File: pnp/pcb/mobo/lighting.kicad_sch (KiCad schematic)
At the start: 2 parts, among them J13 DOWNWARDS_LIGHT, J14 UPWARDS_LIGHT

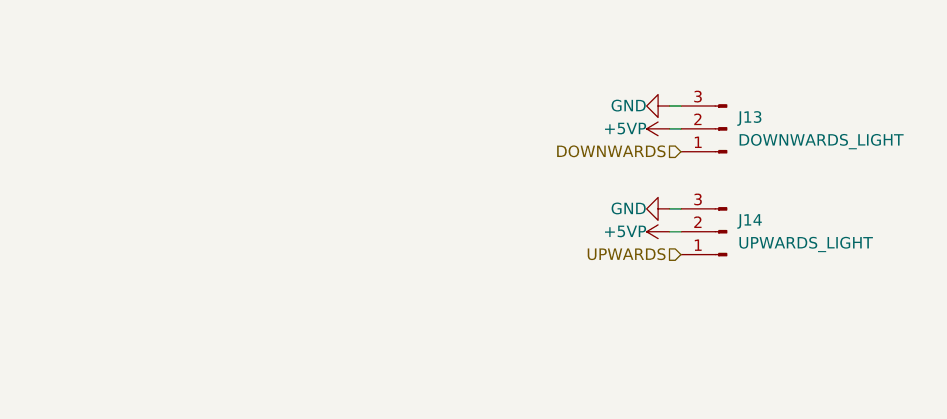
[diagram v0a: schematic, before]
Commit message: Mobo V4A Redesign
Some EMC improvements to schematics.
Reassigned MCU Pins for HW-PWM support.
Changes are still marked with text in the schematics.
Complete PCB Layout reworked
Status: Needs to be verified, and cleaned up a little, but DRC is running green.
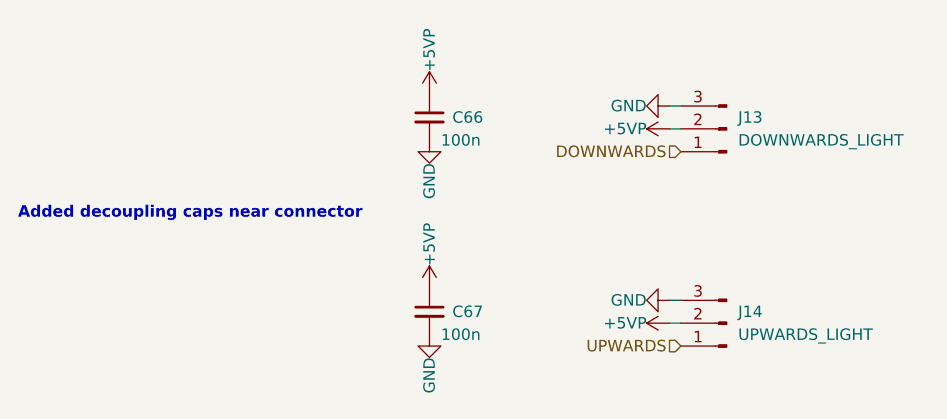
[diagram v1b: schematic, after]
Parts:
- added C66, C67: 100n, Capacitor_SMD:C_0805_2012Metric, symbol Device:C_Small
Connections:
- net +5VP: now also C66.1, C67.1
- net GND: now also C66.2, C67.2
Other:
- note added: "Added decoupling caps near connector"
- moved on the sheet: J14
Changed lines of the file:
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@@
   (title_block
     (title "LumenPnP Motherboard")
-    (date "2022-03-29")
+    (date "2022-09-09")
+    (rev "004A")
     (company "Opulo")
-  )
-  (wire (pts (xy 143.51 105.41) (xy 144.78 105.41))
+    (comment 1 "Reengineered by Magpie")
+  )
+  (wire (pts (xy 143.51 115.57) (xy 144.78 115.57))
     (stroke (width 0) (type default) (color 0 0 0 0))
   )
@@
     (stroke (width 0) (type default) (color 0 0 0 0))
   )
-  (wire (pts (xy 143.51 107.95) (xy 144.78 107.95))
+  (wire (pts (xy 143.51 118.11) (xy 144.78 118.11))
     (stroke (width 0) (type default) (color 0 0 0 0))
   )
@@
     (stroke (width 0) (type default) (color 0 0 0 0))
   )
-  (hierarchical_label "UPWARDS" (shape input) (at 144.78 110.49 180)
+  (text "Added decoupling caps near connector" (at 71.12 106.68 0)
+    (effects (font (size 1.27 1.27) (thickness 0.254) bold) (justify left bottom))
+  )
+  (hierarchical_label "UPWARDS" (shape input) (at 144.78 120.65 180)
     (effects (font (size 1.27 1.27)) (justify right))
   )
@@
     (pin "3")
   )
-  (symbol (lib_id "Connector:Conn_01x03_Male") (at 149.86 107.95 180) (unit 1)
-    (in_bom yes) (on_board yes)
-    (property "Reference" "J14" (id 0) (at 151.13 106.68 0)
-      (effects (font (size 1.27 1.27)) (justify right))
-    )
-    (property "Value" "UPWARDS_LIGHT" (id 1) (at 151.13 109.22 0)
-      (effects (font (size 1.27 1.27)) (justify right))
-    )
-    (property "Footprint" "Connector_JST:JST_XH_B3B-XH-A_1x03_P2.50mm_Vertical" (id 2) (at 149.86 107.95 0)
-      (effects (font (size 1.27 1.27)) hide)
-    )
-    (property "Datasheet" "" (id 3) (at 149.86 107.95 0)
-      (effects (font (size 1.27 1.27)) hide)
-    )
-    (property "LCSC" "C2316" (id 4) (at 149.86 107.95 0)
-      (effects (font (size 1.27 1.27)) hide)
-    )
-    (property "JLCPCB" "C2316" (id 5) (at 149.86 107.95 0)
-      (effects (font (size 1.27 1.27)) hide)
-    )
-    (property "Digikey" "455-2248-ND" (id 6) (at 149.86 107.95 0)
+  (symbol (lib_id "Connector:Conn_01x03_Male") (at 149.86 118.11 180) (unit 1)
+    (in_bom yes) (on_board yes)
+    (property "Reference" "J14" (id 0) (at 151.13 116.84 0)
+      (effects (font (size 1.27 1.27)) (justify right))
+    )
+    (property "Value" "UPWARDS_LIGHT" (id 1) (at 151.13 119.38 0)
+      (effects (font (size 1.27 1.27)) (justify right))
+    )
+    (property "Footprint" "Connector_JST:JST_XH_B3B-XH-A_1x03_P2.50mm_Vertical" (id 2) (at 149.86 118.11 0)
+      (effects (font (size 1.27 1.27)) hide)
+    )
+    (property "Datasheet" "" (id 3) (at 149.86 118.11 0)
+      (effects (font (size 1.27 1.27)) hide)
+    )
+    (property "LCSC" "C2316" (id 4) (at 149.86 118.11 0)
+      (effects (font (size 1.27 1.27)) hide)
+    )
+    (property "JLCPCB" "C2316" (id 5) (at 149.86 118.11 0)
+      (effects (font (size 1.27 1.27)) hide)
+    )
+    (property "Digikey" "455-2248-ND" (id 6) (at 149.86 118.11 0)
       (effects (font (size 1.27 1.27)) hide)
     )
@@
     (pin "3")
   )
+  (symbol (lib_id "power:GND") (at 116.84 97.79 0) (unit 1)
+    (in_bom yes) (on_board yes)
+    (property "Reference" "#PWR023" (id 0) (at 116.84 104.14 0)
+      (effects (font (size 1.27 1.27)) hide)
+    )
+    (property "Value" "GND" (id 1) (at 116.84 100.33 90)
+      (effects (font (size 1.27 1.27)) (justify right))
+    )
+    (property "Footprint" "" (id 2) (at 116.84 97.79 0)
+      (effects (font (size 1.27 1.27)) hide)
+    )
+    (property "Datasheet" "" (id 3) (at 116.84 97.79 0)
+      (effects (font (size 1.27 1.27)) hide)
+    )
+    (pin "1")
+  )
+  (symbol (lib_id "Device:C_Small") (at 116.84 116.84 0) (unit 1)
+    (in_bom yes) (on_board yes)
+    (property "Reference" "C67" (id 0) (at 119.38 116.84 0)
+      (effects (font (size 1.27 1.27)) (justify left))
+    )
+    (property "Value" "100n" (id 1) (at 118.11 119.38 0)
+      (effects (font (size 1.27 1.27)) (justify left))
+    )
+    (property "Footprint" "Capacitor_SMD:C_0805_2012Metric" (id 2) (at 116.84 116.84 0)
+      (effects (font (size 1.27 1.27)) hide)
+    )
+    (property "Datasheet" "" (id 3) (at 116.84 116.84 0)
+      (effects (font (size 1.27 1.27)) hide)
+    )
+    (property "Digikey" "1276-1180-1-ND" (id 4) (at 116.84 116.84 0)
+      (effects (font (size 1.27 1.27)) hide)
+    )
+    (property "JLCPCB" "C49678" (id 5) (at 116.84 116.84 0)
+      (effects (font (size 1.27 1.27)) hide)
+    )
+    (property "LCSC" "C360619" (id 6) (at 116.84 116.84 0)
+      (effects (font (size 1.27 1.27)) hide)
+    )
+    (property "Mouser" "581-08055C104K" (id 7) (at 116.84 116.84 0)
+      (effects (font (size 1.27 1.27)) hide)
+    )
+    (pin "1")
+    (pin "2")
+  )
+  (symbol (lib_id "Device:C_Small") (at 116.84 95.25 0) (unit 1)
+    (in_bom yes) (on_board yes)
+    (property "Reference" "C66" (id 0) (at 119.38 95.25 0)
+      (effects (font (size 1.27 1.27)) (justify left))
+    )
+    (property "Value" "100n" (id 1) (at 118.11 97.79 0)
+      (effects (font (size 1.27 1.27)) (justify left))
+    )
+    (property "Footprint" "Capacitor_SMD:C_0805_2012Metric" (id 2) (at 116.84 95.25 0)
+      (effects (font (size 1.27 1.27)) hide)
+    )
+    (property "Datasheet" "" (id 3) (at 116.84 95.25 0)
+      (effects (font (size 1.27 1.27)) hide)
+    )
+    (property "Digikey" "1276-1180-1-ND" (id 4) (at 116.84 95.25 0)
+      (effects (font (size 1.27 1.27)) hide)
+    )
+    (property "JLCPCB" "C49678" (id 5) (at 116.84 95.25 0)
+      (effects (font (size 1.27 1.27)) hide)
+    )
+    (property "LCSC" "C360619" (id 6) (at 116.84 95.25 0)
+      (effects (font (size 1.27 1.27)) hide)
+    )
+    (property "Mouser" "581-08055C104K" (id 7) (at 116.84 95.25 0)
+      (effects (font (size 1.27 1.27)) hide)
+    )
+    (pin "1")
+    (pin "2")
+  )
   (symbol (lib_id "power:+5VP") (at 143.51 96.52 90) (unit 1)
     (in_bom yes) (on_board yes)
@@
     (pin "1")
   )
+  (symbol (lib_id "power:GND") (at 116.84 119.38 0) (unit 1)
+    (in_bom yes) (on_board yes)
+    (property "Reference" "#PWR025" (id 0) (at 116.84 125.73 0)
+      (effects (font (size 1.27 1.27)) hide)
+    )
+    (property "Value" "GND" (id 1) (at 116.84 121.92 90)
+      (effects (font (size 1.27 1.27)) (justify right))
+    )
+    (property "Footprint" "" (id 2) (at 116.84 119.38 0)
+      (effects (font (size 1.27 1.27)) hide)
+    )
+    (property "Datasheet" "" (id 3) (at 116.84 119.38 0)
+      (effects (font (size 1.27 1.27)) hide)
+    )
+    (pin "1")
+  )
+  (symbol (lib_id "power:+5VP") (at 116.84 92.71 0) (unit 1)
+    (in_bom yes) (on_board yes)
+    (property "Reference" "#PWR013" (id 0) (at 116.84 96.52 0)
+      (effects (font (size 1.27 1.27)) hide)
+    )
+    (property "Value" "+5VP" (id 1) (at 116.84 90.17 90)
+      (effects (font (size 1.27 1.27)) (justify left))
+    )
+    (property "Footprint" "" (id 2) (at 116.84 92.71 0)
+      (effects (font (size 1.27 1.27)) hide)
+    )
+    (property "Datasheet" "" (id 3) (at 116.84 92.71 0)
+      (effects (font (size 1.27 1.27)) hide)
+    )
+    (pin "1")
+  )
+  (symbol (lib_id "power:+5VP") (at 116.84 114.3 0) (unit 1)
+    (in_bom yes) (on_board yes)
+    (property "Reference" "#PWR024" (id 0) (at 116.84 118.11 0)
+      (effects (font (size 1.27 1.27)) hide)
+    )
+    (property "Value" "+5VP" (id 1) (at 116.84 111.76 90)
+      (effects (font (size 1.27 1.27)) (justify left))
+    )
+    (property "Footprint" "" (id 2) (at 116.84 114.3 0)
+      (effects (font (size 1.27 1.27)) hide)
+    )
+    (property "Datasheet" "" (id 3) (at 116.84 114.3 0)
+      (effects (font (size 1.27 1.27)) hide)
+    )
+    (pin "1")
+  )
   (symbol (lib_id "power:GND") (at 143.51 93.98 270) (unit 1)
     (in_bom yes) (on_board yes)
@@
     (pin "1")
   )
-  (symbol (lib_id "power:GND") (at 143.51 105.41 270) (unit 1)
-    (in_bom yes) (on_board yes)
-    (property "Reference" "#PWR0164" (id 0) (at 137.16 105.41 0)
-      (effects (font (size 1.27 1.27)) hide)
-    )
-    (property "Value" "GND" (id 1) (at 140.97 105.41 90)
-      (effects (font (size 1.27 1.27)) (justify right))
-    )
-    (property "Footprint" "" (id 2) (at 143.51 105.41 0)
-      (effects (font (size 1.27 1.27)) hide)
-    )
-    (property "Datasheet" "" (id 3) (at 143.51 105.41 0)
-      (effects (font (size 1.27 1.27)) hide)
-    )
-    (pin "1")
-  )
-  (symbol (lib_id "power:+5VP") (at 143.51 107.95 90) (unit 1)
-    (in_bom yes) (on_board yes)
-    (property "Reference" "#PWR0165" (id 0) (at 147.32 107.95 0)
-      (effects (font (size 1.27 1.27)) hide)
-    )
-    (property "Value" "+5VP" (id 1) (at 140.97 107.95 90)
-      (effects (font (size 1.27 1.27)) (justify left))
-    )
-    (property "Footprint" "" (id 2) (at 143.51 107.95 0)
-      (effects (font (size 1.27 1.27)) hide)
-    )
-    (property "Datasheet" "" (id 3) (at 143.51 107.95 0)
-      (effects (font (size 1.27 1.27)) hide)
-    )
+  (symbol (lib_id "power:GND") (at 143.51 115.57 270) (unit 1)
+    (in_bom yes) (on_board yes)
+    (property "Reference" "#PWR0164" (id 0) (at 137.16 115.57 0)
+      (effects (font (size 1.27 1.27)) hide)
+    )
+    (property "Value" "GND" (id 1) (at 140.97 115.57 90)
+      (effects (font (size 1.27 1.27)) (justify right))
+    )
+    (property "Footprint" "" (id 2) (at 143.51 115.57 0)
+      (effects (font (size 1.27 1.27)) hide)
+    )
+    (property "Datasheet" "" (id 3) (at 143.51 115.57 0)
+      (effects (font (size 1.27 1.27)) hide)
+    )
+    (pin "1")
+  )
+  (symbol (lib_id "power:+5VP") (at 143.51 118.11 90) (unit 1)
+    (in_bom yes) (on_board yes)
+    (property "Reference" "#PWR0165" (id 0) (at 147.32 118.11 0)
+      (effects (font (size 1.27 1.27)) hide)
+    )
+    (property "Value" "+5VP" (id 1) (at 140.97 118.11 90)
+      (effects (font (size 1.27 1.27)) (justify left))
+    )
+    (property "Footprint" "" (id 2) (at 143.51 118.11 0)
+      (effects (font (size 1.27 1.27)) hide)
+    )
+    (property "Datasheet" "" (id 3) (at 143.51 118.11 0)
+      (effects (font (size 1.27 1.27)) hide)
+    )

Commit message: Redesign finished
Completed Board redesign and adding more EMC improvements.
Changed all the part numbers to have a Mouser orderable design (except the JST connectors)
All outputs generated
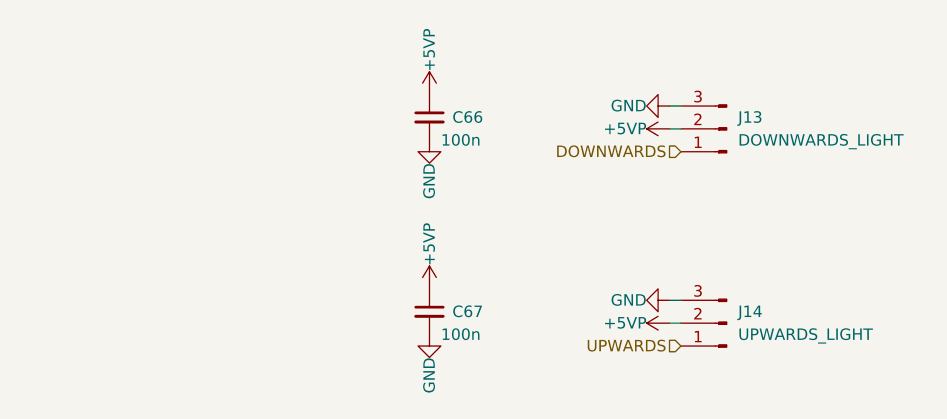
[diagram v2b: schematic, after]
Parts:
- C66, C67: Digikey 1276-1180-1-ND -> (none); JLCPCB C49678 -> (none); LCSC C360619 -> (none); Mouser 581-08055C104K -> 710-885012207098
- J13, J14: JLCPCB C2316 -> (none); LCSC C2316 -> (none); Mouser (none) -> Digikey
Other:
- note removed: "Added decoupling caps near connector"
- company: Opulo -> Opulo.io
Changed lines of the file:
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@@
   (title_block
     (title "LumenPnP Motherboard")
-    (date "2022-09-09")
-    (rev "004A")
-    (company "Opulo")
+    (date "2022-10-06")
+    (rev "04A")
+    (company "Opulo.io")
     (comment 1 "Reengineered by Magpie")
   )
@@
   (wire (pts (xy 143.51 93.98) (xy 144.78 93.98))
     (stroke (width 0) (type default) (color 0 0 0 0))
-  )
-  (text "Added decoupling caps near connector" (at 71.12 106.68 0)
-    (effects (font (size 1.27 1.27) (thickness 0.254) bold) (justify left bottom))
   )
   (hierarchical_label "UPWARDS" (shape input) (at 144.78 120.65 180)
@@
       (effects (font (size 1.27 1.27)) hide)
     )
-    (property "LCSC" "C2316" (id 4) (at 149.86 96.52 0)
+    (property "LCSC" "" (id 4) (at 149.86 96.52 0)
       (effects (font (size 1.27 1.27)) hide)
     )
-    (property "JLCPCB" "C2316" (id 5) (at 149.86 96.52 0)
+    (property "JLCPCB" "" (id 5) (at 149.86 96.52 0)
       (effects (font (size 1.27 1.27)) hide)
     )
     (property "Digikey" "455-2248-ND" (id 6) (at 149.86 96.52 0)
+      (effects (font (size 1.27 1.27)) hide)
+    )
+    (property "Mouser" "Digikey" (id 7) (at 149.86 96.52 0)
       (effects (font (size 1.27 1.27)) hide)
     )
@@
       (effects (font (size 1.27 1.27)) hide)
     )
-    (property "LCSC" "C2316" (id 4) (at 149.86 118.11 0)
+    (property "LCSC" "" (id 4) (at 149.86 118.11 0)
       (effects (font (size 1.27 1.27)) hide)
     )
-    (property "JLCPCB" "C2316" (id 5) (at 149.86 118.11 0)
+    (property "JLCPCB" "" (id 5) (at 149.86 118.11 0)
       (effects (font (size 1.27 1.27)) hide)
     )
     (property "Digikey" "455-2248-ND" (id 6) (at 149.86 118.11 0)
+      (effects (font (size 1.27 1.27)) hide)
+    )
+    (property "Mouser" "Digikey" (id 7) (at 149.86 118.11 0)
       (effects (font (size 1.27 1.27)) hide)
     )
@@
       (effects (font (size 1.27 1.27)) hide)
     )
-    (property "Digikey" "1276-1180-1-ND" (id 4) (at 116.84 116.84 0)
+    (property "Digikey" "" (id 4) (at 116.84 116.84 0)
       (effects (font (size 1.27 1.27)) hide)
     )
-    (property "JLCPCB" "C49678" (id 5) (at 116.84 116.84 0)
+    (property "JLCPCB" "" (id 5) (at 116.84 116.84 0)
       (effects (font (size 1.27 1.27)) hide)
     )
-    (property "LCSC" "C360619" (id 6) (at 116.84 116.84 0)
+    (property "LCSC" "" (id 6) (at 116.84 116.84 0)
       (effects (font (size 1.27 1.27)) hide)
     )
-    (property "Mouser" "581-08055C104K" (id 7) (at 116.84 116.84 0)
+    (property "Mouser" "710-885012207098" (id 7) (at 116.84 116.84 0)
       (effects (font (size 1.27 1.27)) hide)
     )
@@
       (effects (font (size 1.27 1.27)) hide)
     )
-    (property "Digikey" "1276-1180-1-ND" (id 4) (at 116.84 95.25 0)
+    (property "Digikey" "" (id 4) (at 116.84 95.25 0)
       (effects (font (size 1.27 1.27)) hide)
     )
-    (property "JLCPCB" "C49678" (id 5) (at 116.84 95.25 0)
+    (property "JLCPCB" "" (id 5) (at 116.84 95.25 0)
       (effects (font (size 1.27 1.27)) hide)
     )
-    (property "LCSC" "C360619" (id 6) (at 116.84 95.25 0)
+    (property "LCSC" "" (id 6) (at 116.84 95.25 0)
       (effects (font (size 1.27 1.27)) hide)
     )
-    (property "Mouser" "581-08055C104K" (id 7) (at 116.84 95.25 0)
+    (property "Mouser" "710-885012207098" (id 7) (at 116.84 95.25 0)
       (effects (font (size 1.27 1.27)) hide)
     )
